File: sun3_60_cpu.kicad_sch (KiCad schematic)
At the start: 24 parts, among them K199 10UF, U100 68020, U101 68881, U102 PAL16L8, U103 PAL16L8, U104 74F04, U106 PAL16L8, U107 PAL20X10, U108 74F00, U110 40.000 Mhz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

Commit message: Routing
- Initial routing with standard 4 layers setup
- Add SIM holes
- Copper to edge clearance 1.0mm
- Relaxed the layout a little so the autorouter can have results
- Moved K500 to the ethernet section it belongs to, and changed type. Same for K199
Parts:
- K199: footprint Capacitor_THT:CP_Radial_D10.0mm_P5.00mm -> Capacitor_THT:CP_Radial_Tantal_D6.0mm_P2.50mm
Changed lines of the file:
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@@
 			)
 		)
-		(property "Footprint" "Capacitor_THT:CP_Radial_D10.0mm_P5.00mm"
+		(property "Footprint" "Capacitor_THT:CP_Radial_Tantal_D6.0mm_P2.50mm"
 			(at 44.45 176.53 0)
 			(effects
@@
 			)
 		)
-		(property "Datasheet" "~"
+		(property "Datasheet" "https://www.digikey.com/en/products/detail/kyocera-avx/TAP106M035SCS/1471228"
 			(at 44.45 176.53 0)
 			(effects

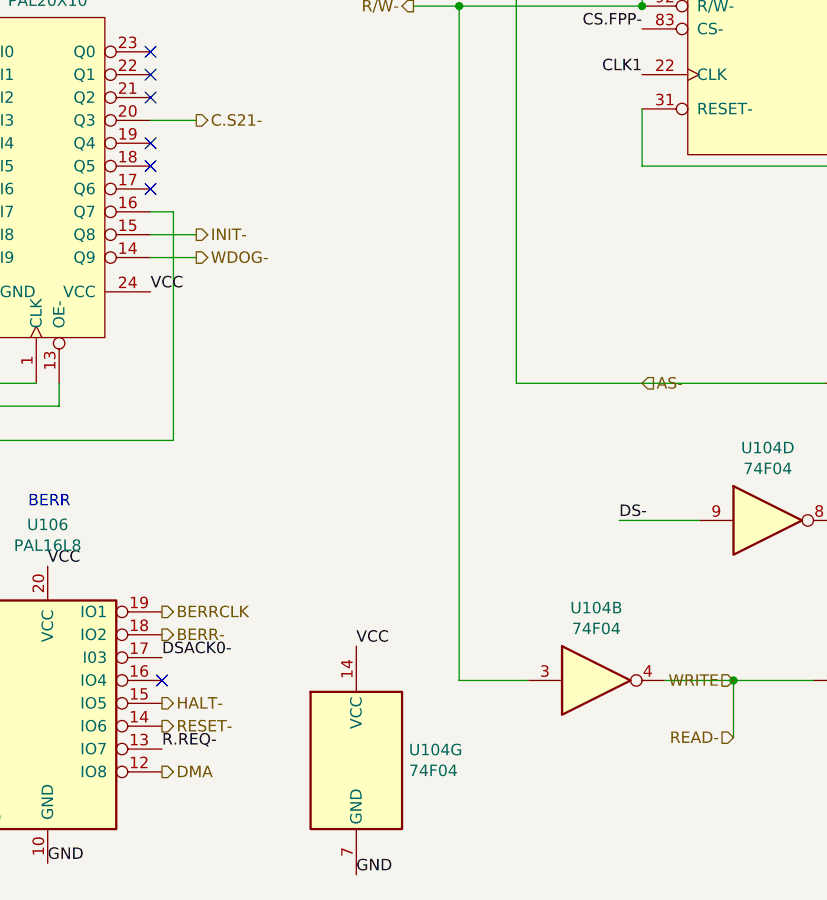
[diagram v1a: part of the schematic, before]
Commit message: Clean up before reorganizing the folders. The schematics and PCB reflect the fixes discovered during the prototype build.
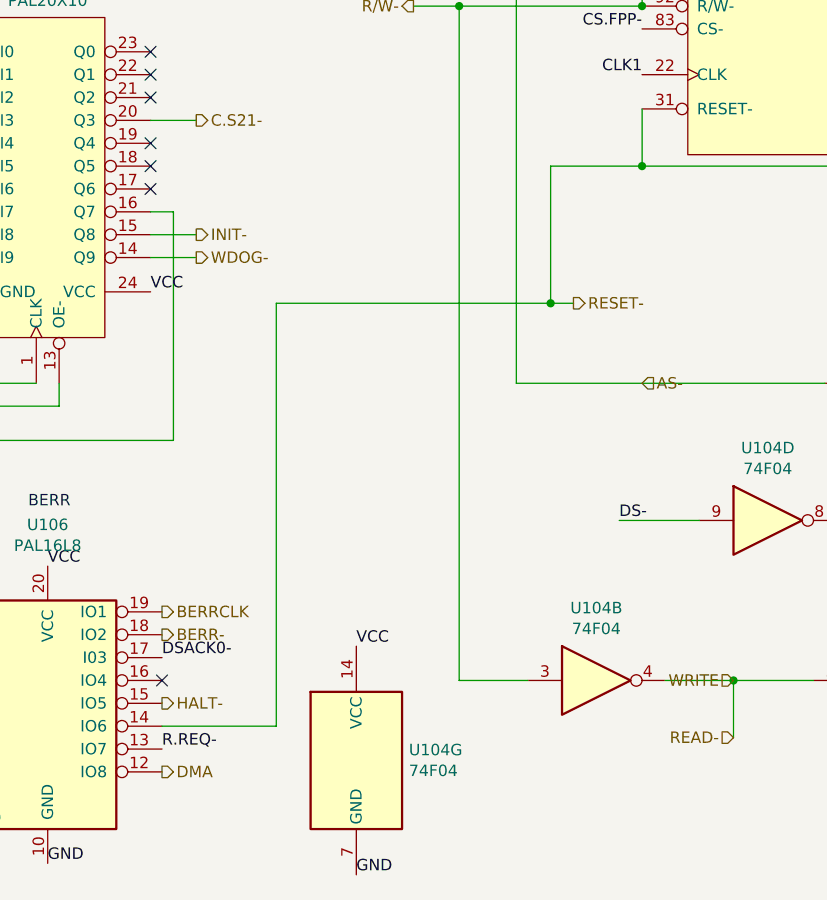
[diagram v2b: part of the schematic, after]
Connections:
- net RESET-: now also U100.27 (RESET-), U101.31 (RESET-)
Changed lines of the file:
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@@
 	)
 	(junction
+		(at 171.45 182.88)
+		(diameter 0)
+		(color 0 0 0 0)
+	)
+	(junction
 		(at 90.17 193.04)
 		(diameter 0)
@@
 	)
 	(junction
+		(at 161.29 198.12)
+		(diameter 0)
+		(color 0 0 0 0)
+	)
+	(junction
 		(at 320.04 85.09)
 		(diameter 0)
@@
 	(wire
 		(pts
+			(xy 163.83 198.12) (xy 161.29 198.12)
+		)
+		(stroke
+			(width 0)
+			(type default)
+		)
+	)
+	(wire
+		(pts
 			(xy 226.06 195.58) (xy 223.52 195.58)
 		)
@@
 	(wire
 		(pts
+			(xy 161.29 182.88) (xy 161.29 198.12)
+		)
+		(stroke
+			(width 0)
+			(type default)
+		)
+	)
+	(wire
+		(pts
 			(xy 83.82 120.65) (xy 83.82 133.35)
 		)
@@
 	(wire
 		(pts
+			(xy 130.81 245.11) (xy 118.11 245.11)
+		)
+		(stroke
+			(width 0)
+			(type default)
+		)
+	)
+	(wire
+		(pts
 			(xy 269.24 40.64) (xy 276.86 40.64)
 		)
@@
 	(wire
 		(pts
+			(xy 171.45 182.88) (xy 161.29 182.88)
+		)
+		(stroke
+			(width 0)
+			(type default)
+		)
+	)
+	(wire
+		(pts
 			(xy 354.33 198.12) (xy 359.41 198.12)
 		)
@@
 		)
 	)
+	(wire
+		(pts
+			(xy 130.81 198.12) (xy 130.81 245.11)
+		)
+		(stroke
+			(width 0)
+			(type default)
+		)
+	)
 	(bus
 		(pts
@@
 	(wire
 		(pts
+			(xy 161.29 198.12) (xy 130.81 198.12)
+		)
+		(stroke
+			(width 0)
+			(type default)
+		)
+	)
+	(wire
+		(pts
 			(xy 247.65 58.42) (xy 255.27 58.42)
 		)
@@
 	(hierarchical_label "RESET-"
 		(shape output)
-		(at 118.11 245.11 0)
+		(at 163.83 198.12 0)
 		(effects
 			(font
